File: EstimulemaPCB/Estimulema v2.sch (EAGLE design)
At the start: 157 parts, among them IC3 74AC14N, IC4 ISO7240S, J1 JUMPERS12MM, J2 J15MM, J3 J_7MM, J4 JUMPERS5MM, J5 JUMPERS7MM, J6 J7MM, K2 HC-06, Q17 TIP48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

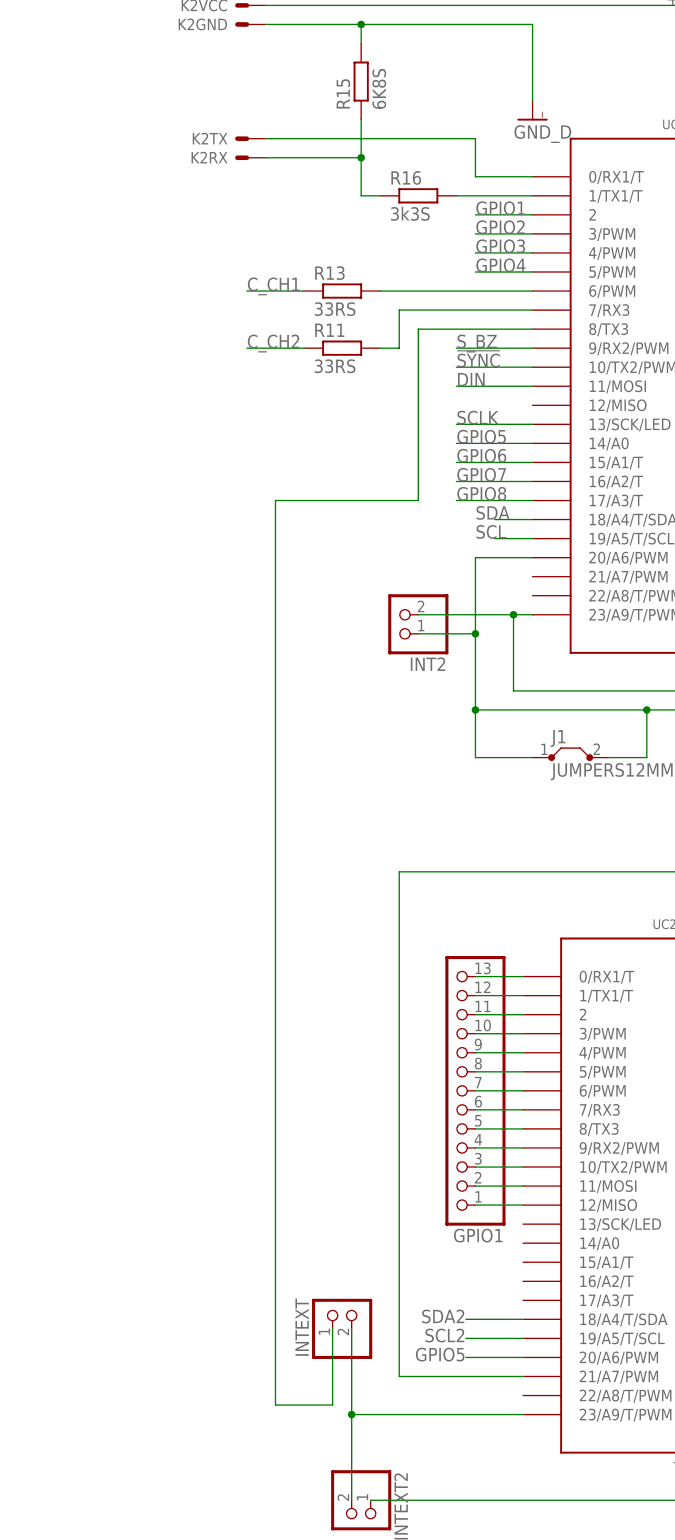
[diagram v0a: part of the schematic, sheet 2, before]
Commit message: Nueva version del estimulema ino
Version v4 con rampa algunos errores por arreglar
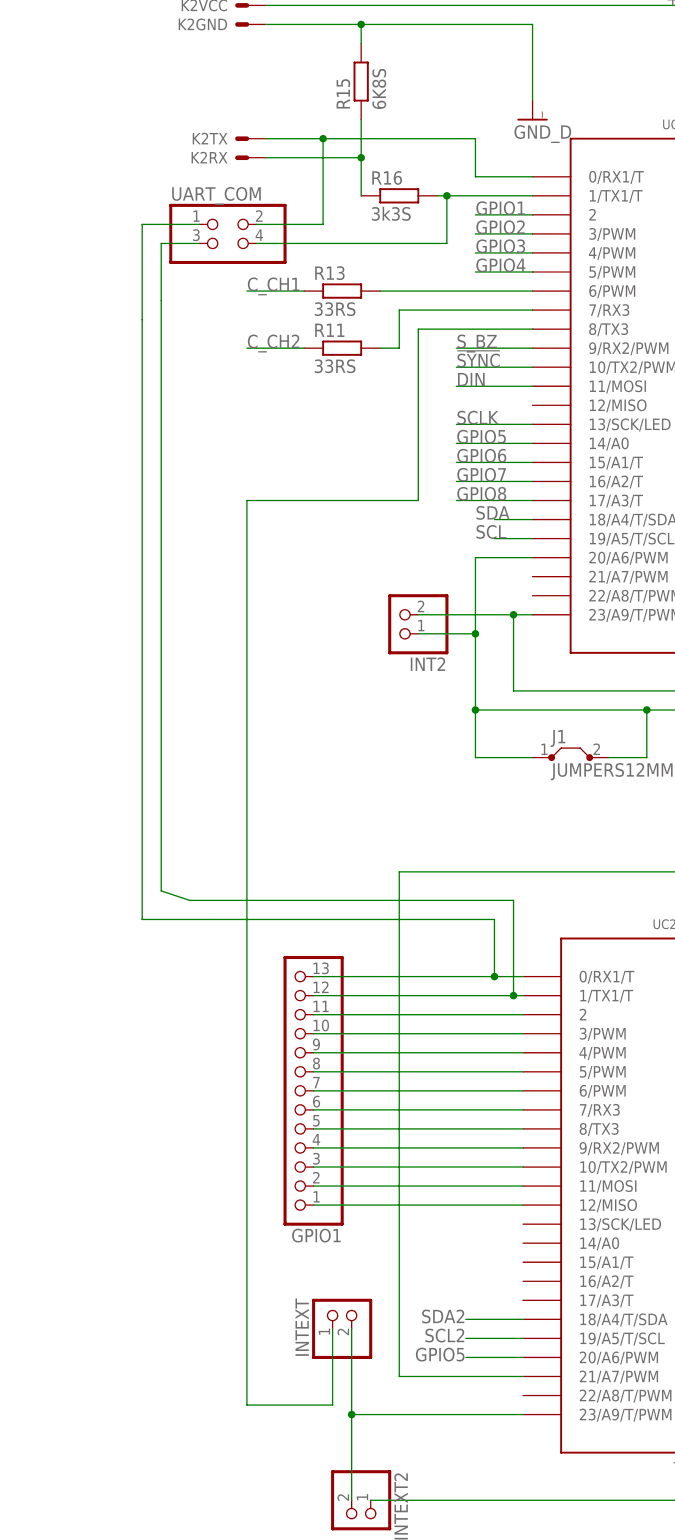
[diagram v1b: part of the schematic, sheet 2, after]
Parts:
- added UART_COM: (no value), pinhead:PINHD-2X2
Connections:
- removed net N$70: R16.2, UC1.1/TX1/T
- removed net N$71: K2TX.S, UC1.0/RX1/T
- new net N$36: R16.2, UART_COM.4, UC1.1/TX1/T
- new net N$38: K2TX.S, UART_COM.2, UC1.0/RX1/T
- net N$6: now also UART_COM.1
- net N$7: now also UART_COM.3
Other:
- moved on the sheet: GPIO1, R16

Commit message: Actualizacion de PCB
Version corregida con todo
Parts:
- added GPIO2_ACCEL: (no value), pinhead:PINHD-1X4
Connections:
- new net N$37: GPIO2_ACCEL.4, UC2.13/SCK/LED
- new net N$39: GPIO2_ACCEL.3, UC2.14/A0
- new net N$40: GPIO2_ACCEL.2, UC2.15/A1/T
- net N$1: now also GPIO2_ACCEL.1

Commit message: Version final estimulema
con ch1 funcionando con rampa, actualizado pcb y nueva version de estimula a la fecha, ademas de algunos modelos 3d
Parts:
- removed X4: (no value), con-ptr500:AK300/3
- added 1: CONECTOR_3_PTR500, 7DI Library:CONECTOR_3_PTR500
- RG1, RG3: device linear:7805TV -> 7DI Library:78XX_V2
- RG2, RG4: device linear:7818TV -> 7DI Library:78XX_V2
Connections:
- net +15_HV: now also 1G$1.KL; no longer X4-1.KL
- net -15: now also 1G$3.KL; no longer X4-3.KL
- net GND_HV: now also 1G$2.KL, K_CH3P1.S, K_CH4P1.S; no longer K_CH3P2.S, K_CH4P2.S, X4-2.KL
- net N$18: now also K_CH3P2.S; no longer K_CH3P1.S
- net N$25: now also K_CH4P2.S; no longer K_CH4P1.S

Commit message: update pcb estimulema v2
cerregidos alguns errores que tenia la pcb
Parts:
- 1: value CONECTOR_3_PTR500 -> PTR500
- R19: value 1K -> 820r
- R27: value 1K -> 820R
- VR1, VR2, VR3, VR4: value 150R -> 500R
- VR10, VR6: value 2k -> 2K
- VR5, VR9: value TRP -> 1K
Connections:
- removed net GNDI: C3.1, IC4.GND1@1, IC4.GND1@2
- net GND_D: now also C3.1, IC4.GND1@1, IC4.GND1@2
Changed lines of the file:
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@@
 <part name="C20" library="7DI Library" library_urn="urn:adsk.eagle:library:1229688" deviceset="CAP_CERAMICO" device="_SMD" package3d_urn="urn:adsk.eagle:package:1281702/2" value="100nf"/>
 <part name="PE15" library="7DI Library" library_urn="urn:adsk.eagle:library:1229688" deviceset="GND_HV" device=""/>
-<part name="VR5" library="7DI Library" library_urn="urn:adsk.eagle:library:1229688" deviceset="TRIMPOT" device="_TH" package3d_urn="urn:adsk.eagle:package:1360028/4" value="TRP"/>
-<part name="VR6" library="7DI Library" library_urn="urn:adsk.eagle:library:1229688" deviceset="TRIMPOT" device="_TH" package3d_urn="urn:adsk.eagle:package:1360028/4" value="2k"/>
+<part name="VR5" library="7DI Library" library_urn="urn:adsk.eagle:library:1229688" deviceset="TRIMPOT" device="_TH" package3d_urn="urn:adsk.eagle:package:1360028/5" value="1K"/>
+<part name="VR6" library="7DI Library" library_urn="urn:adsk.eagle:library:1229688" deviceset="TRIMPOT" device="_TH" package3d_urn="urn:adsk.eagle:package:1360028/5" value="2K"/>
 <part name="R42" library="7DI Library" library_urn="urn:adsk.eagle:library:1229688" deviceset="RESISTOR" device="SMD_0805" package3d_urn="urn:adsk.eagle:package:1282003/2" value="270R"/>
 <part name="PE16" library="7DI Library" library_urn="urn:adsk.eagle:library:1229688" deviceset="GND_HV" device=""/>
@@
 <part name="C32" library="7DI Library" library_urn="urn:adsk.eagle:library:1229688" deviceset="CAP_CERAMICO" device="_SMD" package3d_urn="urn:adsk.eagle:package:1281702/2" value="100nf"/>
 <part name="PE29" library="7DI Library" library_urn="urn:adsk.eagle:library:1229688" deviceset="GND_HV" device=""/>
-<part name="VR9" library="7DI Library" library_urn="urn:adsk.eagle:library:1229688" deviceset="TRIMPOT" device="_TH" package3d_urn="urn:adsk.eagle:package:1360028/4" value="TRP"/>
-<part name="VR10" library="7DI Library" library_urn="urn:adsk.eagle:library:1229688" deviceset="TRIMPOT" device="_TH" package3d_urn="urn:adsk.eagle:package:1360028/4" value="2k"/>
+<part name="VR9" library="7DI Library" library_urn="urn:adsk.eagle:library:1229688" deviceset="TRIMPOT" device="_TH" package3d_urn="urn:adsk.eagle:package:1360028/5" value="1K"/>
+<part name="VR10" library="7DI Library" library_urn="urn:adsk.eagle:library:1229688" deviceset="TRIMPOT" device="_TH" package3d_urn="urn:adsk.eagle:package:1360028/5" value="2K"/>
 <part name="R58" library="7DI Library" library_urn="urn:adsk.eagle:library:1229688" deviceset="RESISTOR" device="SMD_0805" package3d_urn="urn:adsk.eagle:package:1282003/2" value="270R"/>
 <part name="PE30" library="7DI Library" library_urn="urn:adsk.eagle:library:1229688" deviceset="GND_HV" device=""/>
@@
 <part name="R1" library="7DI Library" library_urn="urn:adsk.eagle:library:1229688" deviceset="RESISTOR" device="T_LARGO" package3d_urn="urn:adsk.eagle:package:1232752/4" value="10RS"/>
 <part name="R5" library="7DI Library" library_urn="urn:adsk.eagle:library:1229688" deviceset="RESISTOR" device="T_LARGO" package3d_urn="urn:adsk.eagle:package:1232752/4" value="10RS"/>
-<part name="VR1" library="7DI Library" library_urn="urn:adsk.eagle:library:1229688" deviceset="TRIMPOT" device="_TH" package3d_urn="urn:adsk.eagle:package:1360028/4" value="150R"/>
-<part name="VR2" library="7DI Library" library_urn="urn:adsk.eagle:library:1229688" deviceset="TRIMPOT" device="_TH" package3d_urn="urn:adsk.eagle:package:1360028/4" value="150R"/>
-<part name="VR3" library="7DI Library" library_urn="urn:adsk.eagle:library:1229688" deviceset="TRIMPOT" device="_TH" package3d_urn="urn:adsk.eagle:package:1360028/4" value="150R"/>
-<part name="VR4" library="7DI Library" library_urn="urn:adsk.eagle:library:1229688" deviceset="TRIMPOT" device="_TH" package3d_urn="urn:adsk.eagle:package:1360028/4" value="150R"/>
+<part name="VR1" library="7DI Library" library_urn="urn:adsk.eagle:library:1229688" deviceset="TRIMPOT" device="_TH" package3d_urn="urn:adsk.eagle:package:1360028/5" value="500R"/>
+<part name="VR2" library="7DI Library" library_urn="urn:adsk.eagle:library:1229688" deviceset="TRIMPOT" device="_TH" package3d_urn="urn:adsk.eagle:package:1360028/5" value="500R"/>
+<part name="VR3" library="7DI Library" library_urn="urn:adsk.eagle:library:1229688" deviceset="TRIMPOT" device="_TH" package3d_urn="urn:adsk.eagle:package:1360028/5" value="500R"/>
+<part name="VR4" library="7DI Library" library_urn="urn:adsk.eagle:library:1229688" deviceset="TRIMPOT" device="_TH" package3d_urn="urn:adsk.eagle:package:1360028/5" value="500R"/>
 <part name="D1" library="7DI Library" library_urn="urn:adsk.eagle:library:1229688" deviceset="DIODO" device="WEB" package3d_urn="urn:adsk.eagle:package:4574534/2" value="1N4007S"/>
 <part name="D3" library="7DI Library" library_urn="urn:adsk.eagle:library:1229688" deviceset="DIODO" device="WEB" package3d_urn="urn:adsk.eagle:package:4574534/2" value="1N4007S"/>
@@
 <part name="JP10" library="pinhead" library_urn="urn:adsk.eagle:library:325" deviceset="PINHD-1X2" device="" package3d_urn="urn:adsk.eagle:package:22435/2"/>
 <part name="GND_D4" library="supply1" library_urn="urn:adsk.eagle:library:371" deviceset="GNDI" device="" value="GND_D"/>
-<part name="R19" library="7DI Library" library_urn="urn:adsk.eagle:library:1229688" deviceset="RESISTOR" device="SMD_0805" package3d_urn="urn:adsk.eagle:package:1282003/2" value="1K"/>
-<part name="R27" library="7DI Library" library_urn="urn:adsk.eagle:library:1229688" deviceset="RESISTOR" device="SMD_0805" package3d_urn="urn:adsk.eagle:package:1282003/2" value="1K"/>
+<part name="R19" library="7DI Library" library_urn="urn:adsk.eagle:library:1229688" deviceset="RESISTOR" device="SMD_0805" package3d_urn="urn:adsk.eagle:package:1282003/2" value="820r"/>
+<part name="R27" library="7DI Library" library_urn="urn:adsk.eagle:library:1229688" deviceset="RESISTOR" device="SMD_0805" package3d_urn="urn:adsk.eagle:package:1282003/2" value="820R"/>
 <part name="X1HV+" library="7DI Library" library_urn="urn:adsk.eagle:library:1229688" deviceset="CONECTOR_" device="5.08" package3d_urn="urn:adsk.eagle:package:1393551/4"/>
 <part name="X3HV-" library="7DI Library" library_urn="urn:adsk.eagle:library:1229688" deviceset="CONECTOR_" device="5.08" package3d_urn="urn:adsk.eagle:package:1393551/4"/>
@@
 <part name="UART_COM" library="pinhead" library_urn="urn:adsk.eagle:library:325" deviceset="PINHD-2X2" device="" package3d_urn="urn:adsk.eagle:package:22455/2"/>
 <part name="GPIO2_ACCEL" library="pinhead" library_urn="urn:adsk.eagle:library:325" deviceset="PINHD-1X4" device="" package3d_urn="urn:adsk.eagle:package:22407/2"/>
-<part name="1" library="7DI Library" library_urn="urn:adsk.eagle:library:1229688" deviceset="CONECTOR_3_PTR500" device="" package3d_urn="urn:adsk.eagle:package:5402944/3"/>
+<part name="1" library="7DI Library" library_urn="urn:adsk.eagle:library:1229688" deviceset="CONECTOR_3_PTR500" device="" package3d_urn="urn:adsk.eagle:package:5402944/3" value="PTR500"/>
 </parts>
 <sheets>
@@
 </segment>
 </net>
-<net name="GND_HV" class="5">
+<net name="GND_HV" class="1">
 <segment>
 <pinref part="PE39" gate="M" pin="PE"/>
@@
 </segment>
 </net>
-<net name="GNDI" class="3">
-<segment>
-<pinref part="IC4" gate="G$1" pin="GND1@2"/>
-<pinref part="IC4" gate="G$1" pin="GND1@1"/>
-<wire x1="-154.94" y1="-40.64" x2="-154.94" y2="-38.1" width="0.1524" layer="91"/>
-<wire x1="-154.94" y1="-38.1" x2="-149.86" y2="-38.1" width="0.1524" layer="91"/>
-<wire x1="-149.86" y1="-40.64" x2="-154.94" y2="-40.64" width="0.1524" layer="91"/>
-<junction x="-154.94" y="-40.64"/>
-<pinref part="C3" gate="G$1" pin="1"/>
-<wire x1="-167.64" y1="-40.64" x2="-167.64" y2="-7.62" width="0.1524" layer="91"/>
-<wire x1="-165.1" y1="-7.62" x2="-167.64" y2="-7.62" width="0.1524" layer="91"/>
-<wire x1="-154.94" y1="-40.64" x2="-167.64" y2="-40.64" width="0.1524" layer="91"/>
-<wire x1="-167.64" y1="-45.72" x2="-167.64" y2="-40.64" width="0.1524" layer="91"/>
-<junction x="-167.64" y="-40.64"/>
-<pinref part="GND_D11" gate="G$1" pin="GNDI"/>
-</segment>
-</net>
 <net name="N$73" class="2">
 <segment>
@@
 <label x="-57.15" y="82.55" size="1.778" layer="95" rot="R270"/>
 </segment>
+<segment>
+<pinref part="IC4" gate="G$1" pin="GND1@2"/>
+<pinref part="IC4" gate="G$1" pin="GND1@1"/>
+<wire x1="-154.94" y1="-40.64" x2="-154.94" y2="-38.1" width="0.1524" layer="91"/>
+<wire x1="-154.94" y1="-38.1" x2="-149.86" y2="-38.1" width="0.1524" layer="91"/>
+<wire x1="-149.86" y1="-40.64" x2="-154.94" y2="-40.64" width="0.1524" layer="91"/>
+<junction x="-154.94" y="-40.64"/>
+<pinref part="C3" gate="G$1" pin="1"/>
+<wire x1="-167.64" y1="-40.64" x2="-167.64" y2="-7.62" width="0.1524" layer="91"/>
+<wire x1="-165.1" y1="-7.62" x2="-167.64" y2="-7.62" width="0.1524" layer="91"/>
+<wire x1="-154.94" y1="-40.64" x2="-167.64" y2="-40.64" width="0.1524" layer="91"/>
+<wire x1="-167.64" y1="-45.72" x2="-167.64" y2="-40.64" width="0.1524" layer="91"/>
+<junction x="-167.64" y="-40.64"/>
+<pinref part="GND_D11" gate="G$1" pin="GNDI"/>
+</segment>
 </net>
 <net name="+5_D" class="4">
@@
 </segment>
 </net>
-<net name="GND_HV" class="5">
+<net name="GND_HV" class="1">
 <segment>
 <pinref part="IC4" gate="G$1" pin="GND2@1"/>
@@
 </segment>
 </net>
-<net name="GND_HV" class="5">
+<net name="GND_HV" class="1">
 <segment>
 <pinref part="PE16" gate="M" pin="PE"/>
@@
 </segment>
 </net>
-<net name="GND_HV" class="5">
+<net name="GND_HV" class="1">
 <segment>
 <pinref part="PE30" gate="M" pin="PE"/>
@@
 </segment>
 </net>
-<net name="GND_HV" class="5">
+<net name="GND_HV" class="1">
 <segment>
 <pinref part="R12" gate="G$1" pin="2"/>

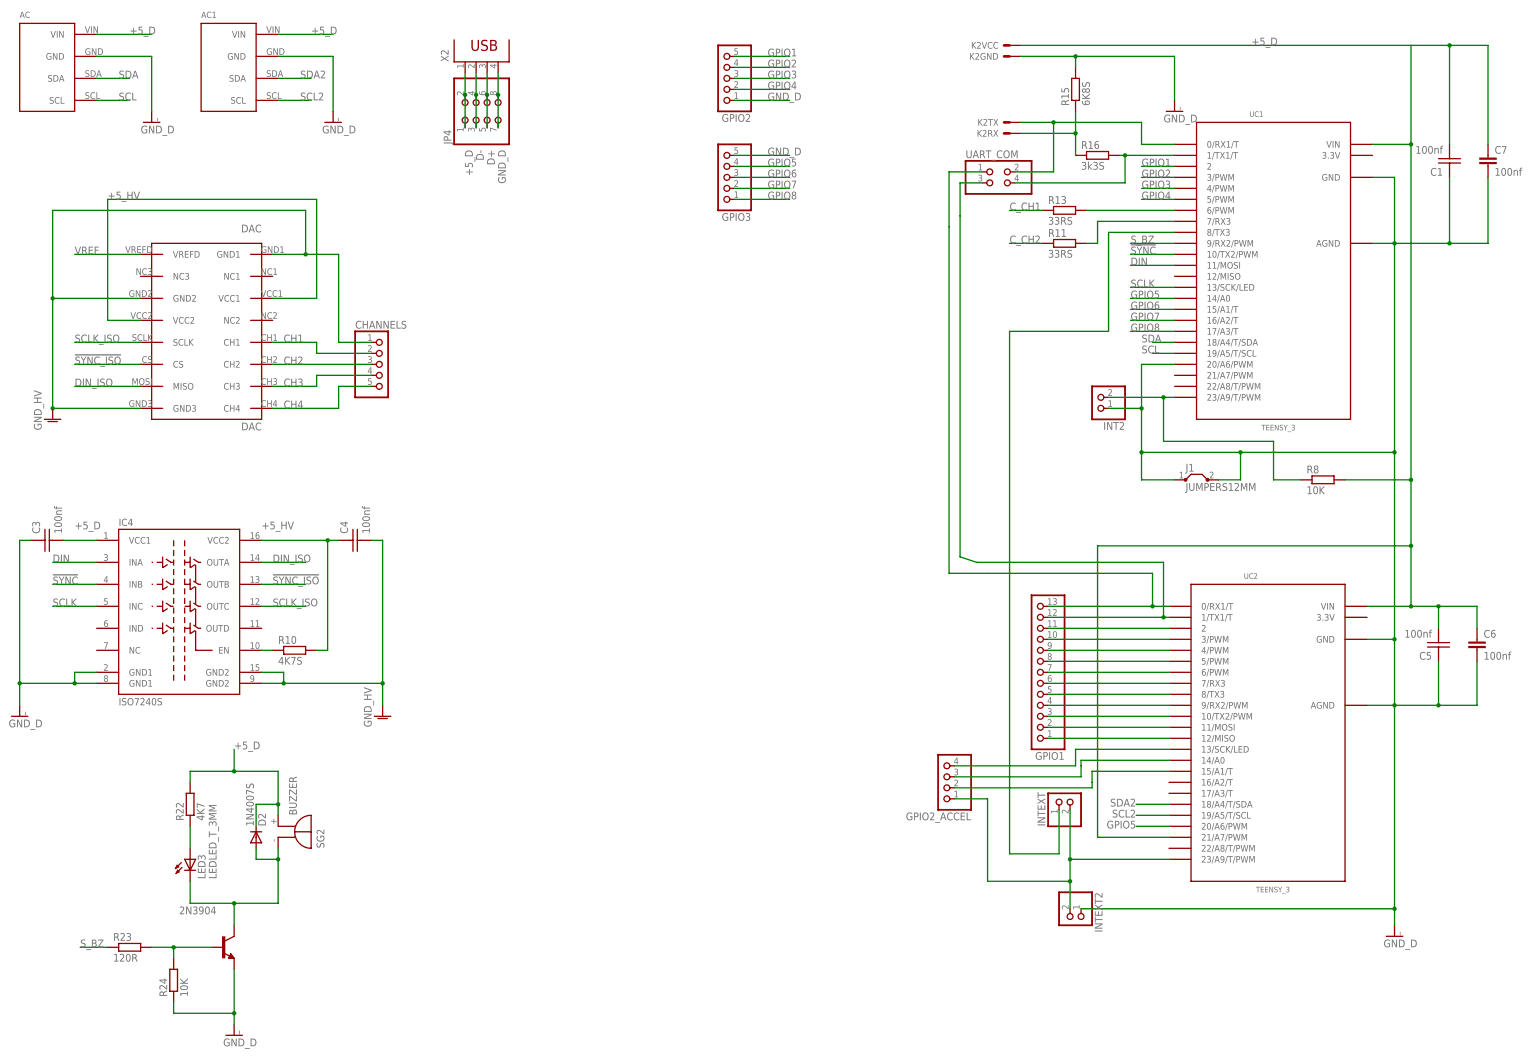
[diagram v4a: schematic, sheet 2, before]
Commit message: Treinamento y acel
Ahora el stim ino y el diag and train pueden capturar datos del entrenamiento al igual que en el test de exitabilidad
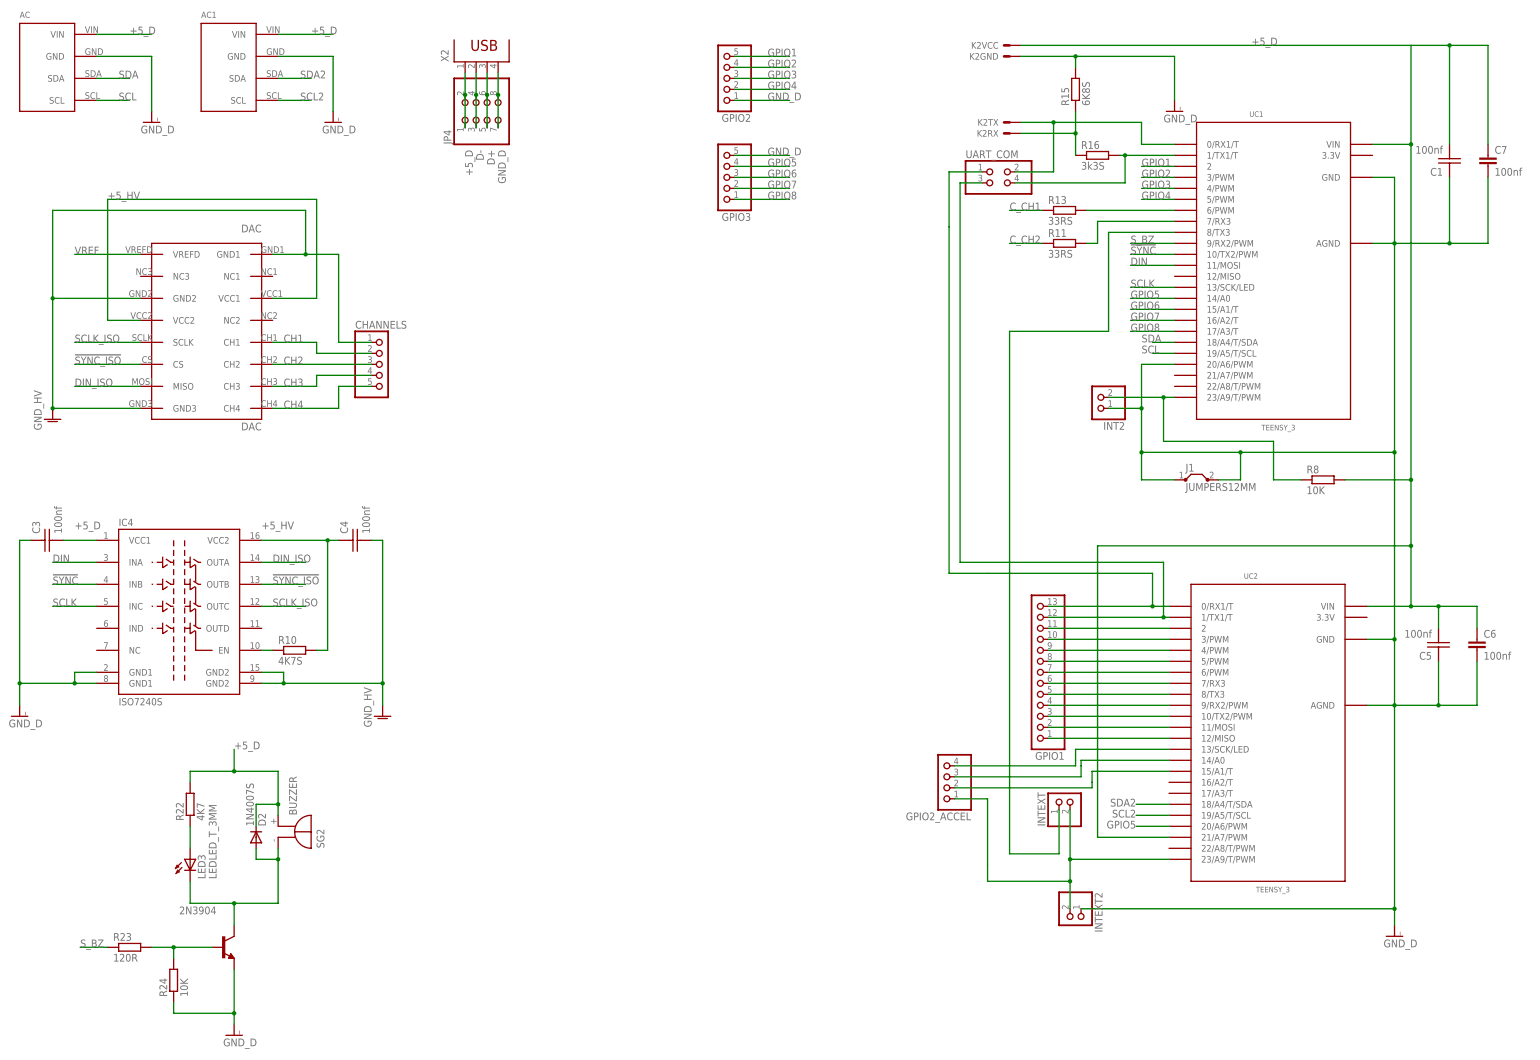
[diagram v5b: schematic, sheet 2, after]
